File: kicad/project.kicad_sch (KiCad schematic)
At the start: 0 parts

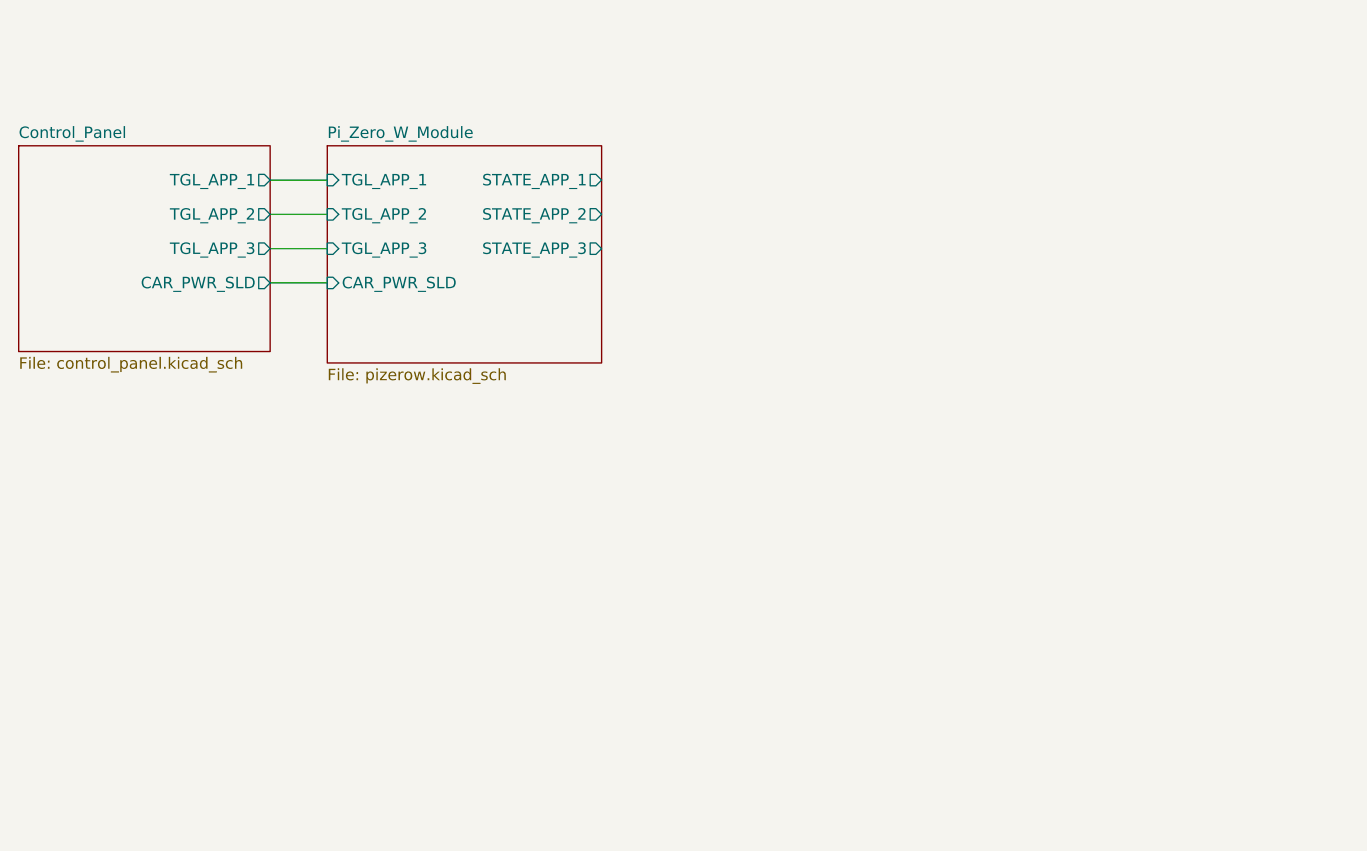
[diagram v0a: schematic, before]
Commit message: developed proper schematic in KiCad along with supporting firmware. code still doesnt gracefully handle all errors but it now does for ureq (network) errors, turning the LAN light off but not ejecting
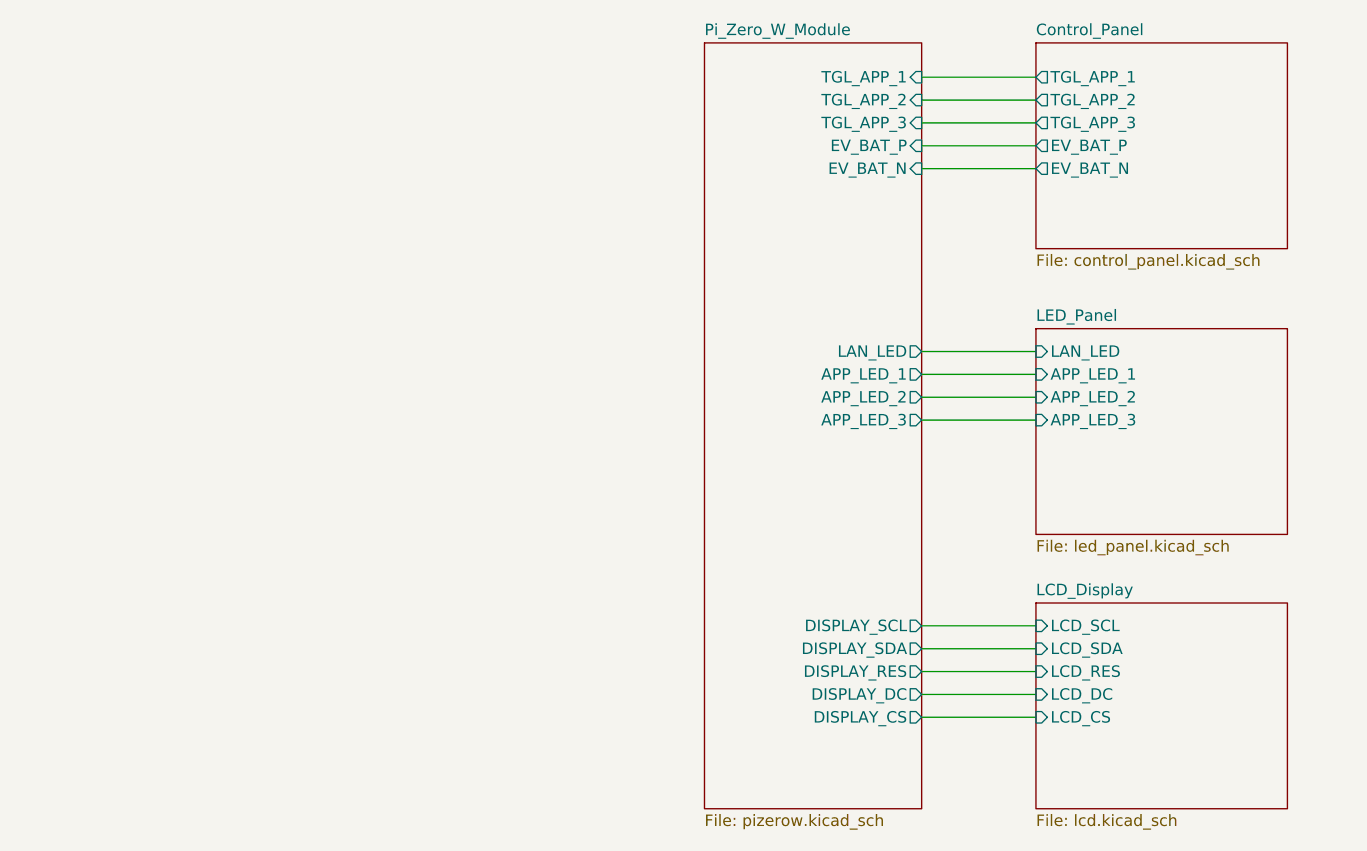
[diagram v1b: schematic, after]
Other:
- added sheet LCD_Display (lcd.kicad_sch)
- added sheet LED_Panel (led_panel.kicad_sch)
- sheet Control_Panel ports: added EV_BAT_N, EV_BAT_P; removed CAR_PWR_SLD
- sheet Pi_Zero_W_Module ports: added APP_LED_1, APP_LED_2, APP_LED_3, DISPLAY_CS, DISPLAY_DC, DISPLAY_RES, DISPLAY_SCL, DISPLAY_SDA, EV_BAT_N, EV_BAT_P, LAN_LED; removed CAR_PWR_SLD, STATE_APP_1, STATE_APP_2, STATE_APP_3
